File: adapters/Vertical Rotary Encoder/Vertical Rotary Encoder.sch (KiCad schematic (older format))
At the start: 4 parts, among them J1 Conn_01x04

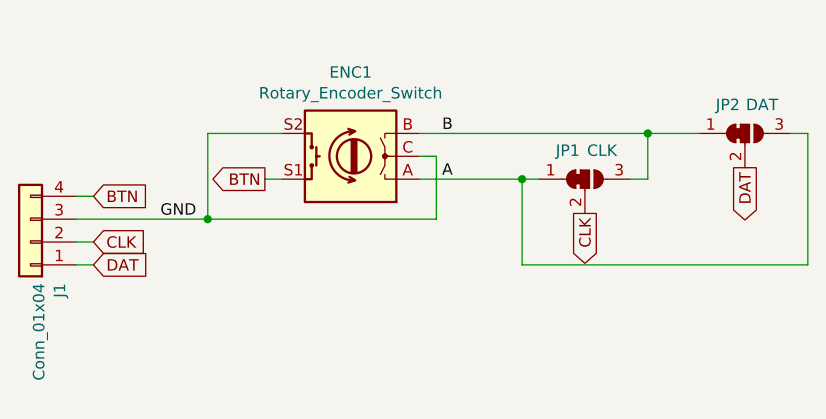
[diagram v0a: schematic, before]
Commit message: Changed default setting to match expected direction
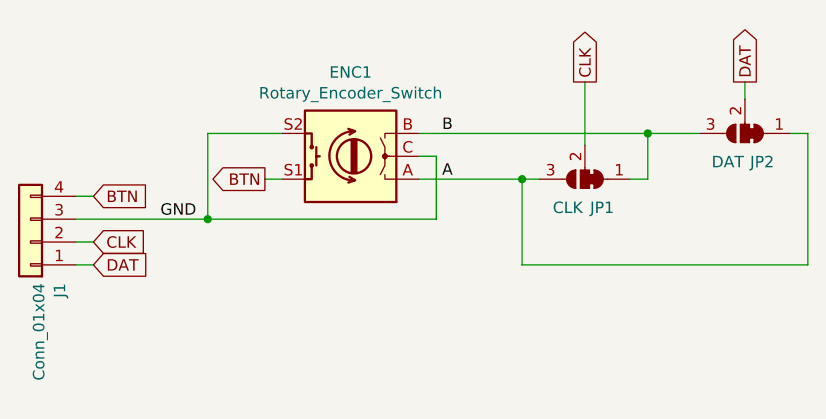
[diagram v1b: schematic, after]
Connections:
- net A: now also JP1.3 (B), JP2.1 (A); no longer JP1.1 (A), JP2.3 (B)
- net B: now also JP1.1 (A), JP2.3 (B); no longer JP1.3 (B), JP2.1 (A)
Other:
- moved on the sheet: JP1, JP2
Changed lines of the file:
@@
 Title "Vertical Rotary Encoder"
 Date ""
-Rev "A"
+Rev "B"
 Comp ""
 Comment1 "Jumpers allow reversing direction."
@@
 F 3 "~" H 6725 3550 50  0001 C CNN
 	1    6725 3550
-	1    0    0    -1
+	-1   0    0    1
 $EndComp
 Text GLabel 5325 3550 0    50   Output ~ 0
@@
 Wire Wire Line
 	5075 3725 6075 3725
-Text GLabel 6725 3700 3    50   Output ~ 0
+Text GLabel 6725 3125 1    50   Output ~ 0
 CLK
 $Comp
@@
 F 3 "~" H 7425 3350 50  0001 C CNN
 	1    7425 3350
-	1    0    0    -1
+	-1   0    0    1
 $EndComp
-Text GLabel 7425 3500 3    50   Output ~ 0
+Text GLabel 7425 3125 1    50   Output ~ 0
 DAT
 Wire Wire Line
@@
 Text Label 6100 3350 0    50   ~ 0
 B
+Wire Wire Line
+	7425 3200 7425 3125
+Wire Wire Line
+	6725 3125 6725 3400
 $EndSCHEMATC
